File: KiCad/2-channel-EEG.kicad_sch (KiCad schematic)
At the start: 77 parts, among them J1 Power_Input, J10 ADC_Data, J11 ISO_IN_C, J12 CH1_AVG_EN, J13 MCU_Data, J14 CH2_AVG_EN, J2 Nucleo_3.3, J3 Electrode_Input, J4 GND_select, J7 Conn_02x01, J8 Conn_02x01, J9 ADC_23, SW1 SW_Push_SPDT, U1 PESE1-S5-S5-M-TR, U10 AD8606, U11 ISO6763-Q1, U2 AD8237, U3 AD8237, U4 AD8606, U5 AD8606, U6 TCR2EF33, U7 AD8606, U8 AD8606, U9 MCP3562R

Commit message: drl filter, additional caps for adc, Rs for adc spi.
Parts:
- removed R20: 2M, Resistor_SMD:R_0805_2012Metric_Pad1.20x1.40mm_HandSolder, symbol Device:R_US
- added C19, C25: 10u, Capacitor_SMD:C_0805_2012Metric_Pad1.18x1.45mm_HandSolder, symbol Device:C_Small
- added C27: 1u, Capacitor_SMD:C_0805_2012Metric_Pad1.18x1.45mm_HandSolder, symbol Device:C_Small
- added R23, R24, R25, R26, R27, R28: 10, Resistor_SMD:R_0805_2012Metric_Pad1.20x1.40mm_HandSolder, symbol Device:R_US
- added R29: 1M, Resistor_SMD:R_0805_2012Metric_Pad1.20x1.40mm_HandSolder, symbol Device:R_US
- C17: value C -> 10u
- C18: value 2u -> 10u
- C20: value 1u -> 10u
- R18: value R -> 100
- renumbered C19 to C21, C21 to C22, C22 to C23, C23 to C24, C24 to C26, C25 to C28, J12 to J10, J13 to J11, J14 to J12, J7 to J5, J8 to J6, J9 to J7, J10 to J8, J11 to J9, R21 to R20, R22 to R21, R23 to R22, U9 to U10, U10 to U9
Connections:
- net +3.3V: now also C20.2, C25.2
- net ADC_MCLK: now also R23.1; no longer U10.18 (MCLK)
- net ADC_SCK: now also R27.1; no longer U10.14 (SCK)
- net ADC_SDI: now also R26.1; no longer U10.15 (SDI)
- net ADC_SDO: now also R25.1; no longer U10.16 (SDO)
- net ADC_~{CS}: now also R28.1; no longer U10.13 (~{CS})
- net ADC_~{IRQ}: now also R24.1; no longer U10.17 (~{IRQ}/MDAT)
- net Driven_GND: now also C22.1, R20.1, R21.1; no longer C20.1
- net GND: now also C20.1, U10.3 (REFIN-), C19.2, C25.1
- net VGND: now also R29.1
- net at J10.1 (Pin_1), J12.1 (Pin_1): now also C27.2; no longer U9.5 (+)
- net at U10.4 (REFIN+/OUT): now also C19.1
- net +3.3V_nucleo renamed +3V3_nucleo
- new net: C27.1, R29.2, U9.5 (+)
- new net: R24.2, U10.17 (~{IRQ}/MDAT)
- new net: R27.2, U10.14 (SCK)
- new net: R26.2, U10.15 (SDI)
- new net: R25.2, U10.16 (SDO)
- new net: R28.2, U10.13 (~{CS})
- new net: R23.2, U10.18 (MCLK)
- no-connect marks 6 -> 4
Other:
- moved on the sheet: C15, C22, C23, J10, J12, R20, R21, R22, RN1, RN2, U7A, U9A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

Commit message: updated DRL and pcb
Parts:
- removed J10: CH1_AVG_EN, Connector_PinHeader_2.54mm:PinHeader_2x01_P2.54mm_Vertical, symbol Connector_Generic:Conn_02x01
- removed J12: CH2_AVG_EN, Connector_PinHeader_2.54mm:PinHeader_2x01_P2.54mm_Vertical, symbol Connector_Generic:Conn_02x01
- removed R20: 60k, Resistor_SMD:R_0805_2012Metric_Pad1.20x1.40mm_HandSolder, symbol Device:R_US
- added C26: 0.1u, Capacitor_SMD:C_0805_2012Metric_Pad1.18x1.45mm_HandSolder, symbol Device:C_Small
- added C29: 1u, Capacitor_SMD:C_0805_2012Metric_Pad1.18x1.45mm_HandSolder, symbol Device:C_Small
- added J7: VGND, Connector_PinHeader_2.54mm:PinHeader_1x01_P2.54mm_Vertical, symbol Connector_Generic:Conn_01x01
- added R22: 10k, Resistor_SMD:R_0805_2012Metric_Pad1.20x1.40mm_HandSolder, symbol Device:R_US
- added R30: 1M, Resistor_SMD:R_0805_2012Metric_Pad1.20x1.40mm_HandSolder, symbol Device:R_US
- added U11: AD8606, Package_SO:MSOP-8_3x3mm_P0.65mm, symbol Senior_Project_Library:AD8606
- renumbered C17 to C16, C18 to C17, C16 to C18, C3 to C2, C26 to C27, C27 to C28, C2 to C3, C28 to C30, C7 to C6, C6 to C7, J9 to J10, J7 to J8, J8 to J9, R3 to R1, R16 to R14, R17 to R15, R14 to R16, R15 to R17, R4 to R2, R21 to R20, R22 to R21, R1 to R3, R2 to R4, R6 to R5, R5 to R6, R8 to R7, R7 to R8, U11 to U12, U3 to U2, U2 to U3, U5 to U4, U4 to U5
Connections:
- net +3.3V: now also C26.2, U11.8 (V+)
- net CH1+: now also J3.4 (Pin_4), RN2.3, U2.2 (+); no longer J3.5 (Pin_5), RN1.3, U3.2 (+)
- net CH1-: now also J3.5 (Pin_5), RN2.4, U2.3 (-); no longer J3.4 (Pin_4), RN1.4, U3.3 (-)
- net CH1_AO: now also C16.2, R18.1; no longer C17.2, R19.1
- net CH2+: now also J3.1 (Pin_1), RN1.3, U3.2 (+); no longer J3.2 (Pin_2), RN2.3, U2.2 (+)
- net CH2-: now also J3.2 (Pin_2), RN1.4, U3.3 (-); no longer J3.1 (Pin_1), RN2.4, U2.3 (-)
- net CH2_AO: now also C17.2, R19.1; no longer C16.2, R18.1
- net Driven_GND: now also U9.1
- net GND: now also C26.1, U11.4 (V-), U11.5 (+)
- net VGND: now also J4.3 (Pin_4), J7.1 (Pin_1), R30.1; no longer J4.4 (Pin_4)
- net at C28.2: now also RN1.1, RN1.2
- net at C22.2, R20.2, U9.2 (-): now also R21.2, R22.1; no longer R21.1
- net at U9.6 (-), U9.7: now also R21.1; no longer R21.2
- net at RN2.1, RN2.2: now also C29.2
- new net: R22.2, U11.1, U11.2 (-)
- new net: U11.6 (-), U11.7
- new net: C29.1, R30.2, U11.3 (+)
- no-connect marks 4 -> 3
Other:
- moved on the sheet: C10, C11, C13, C14, C15, C16, C17, C19, C2, C20, C21, C22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

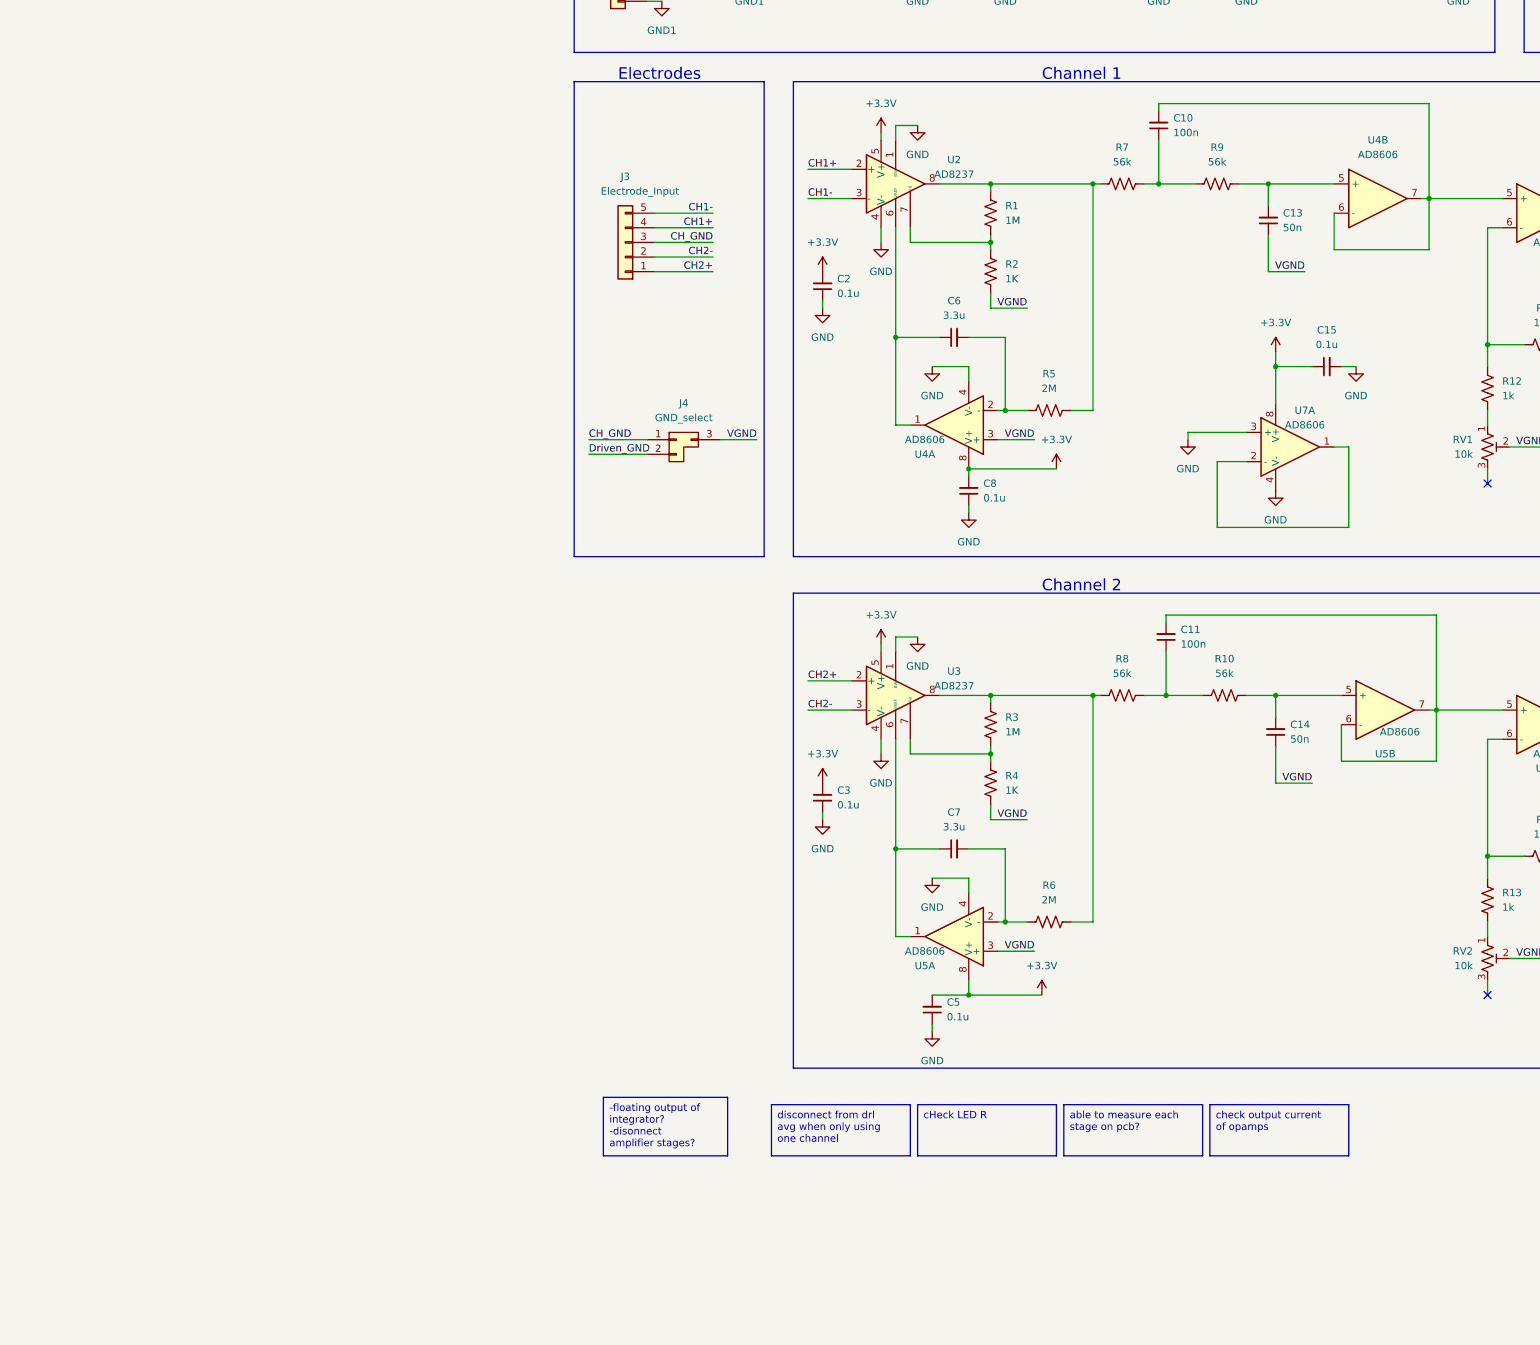
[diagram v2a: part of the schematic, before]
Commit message: added solder jumpers between INA and filter
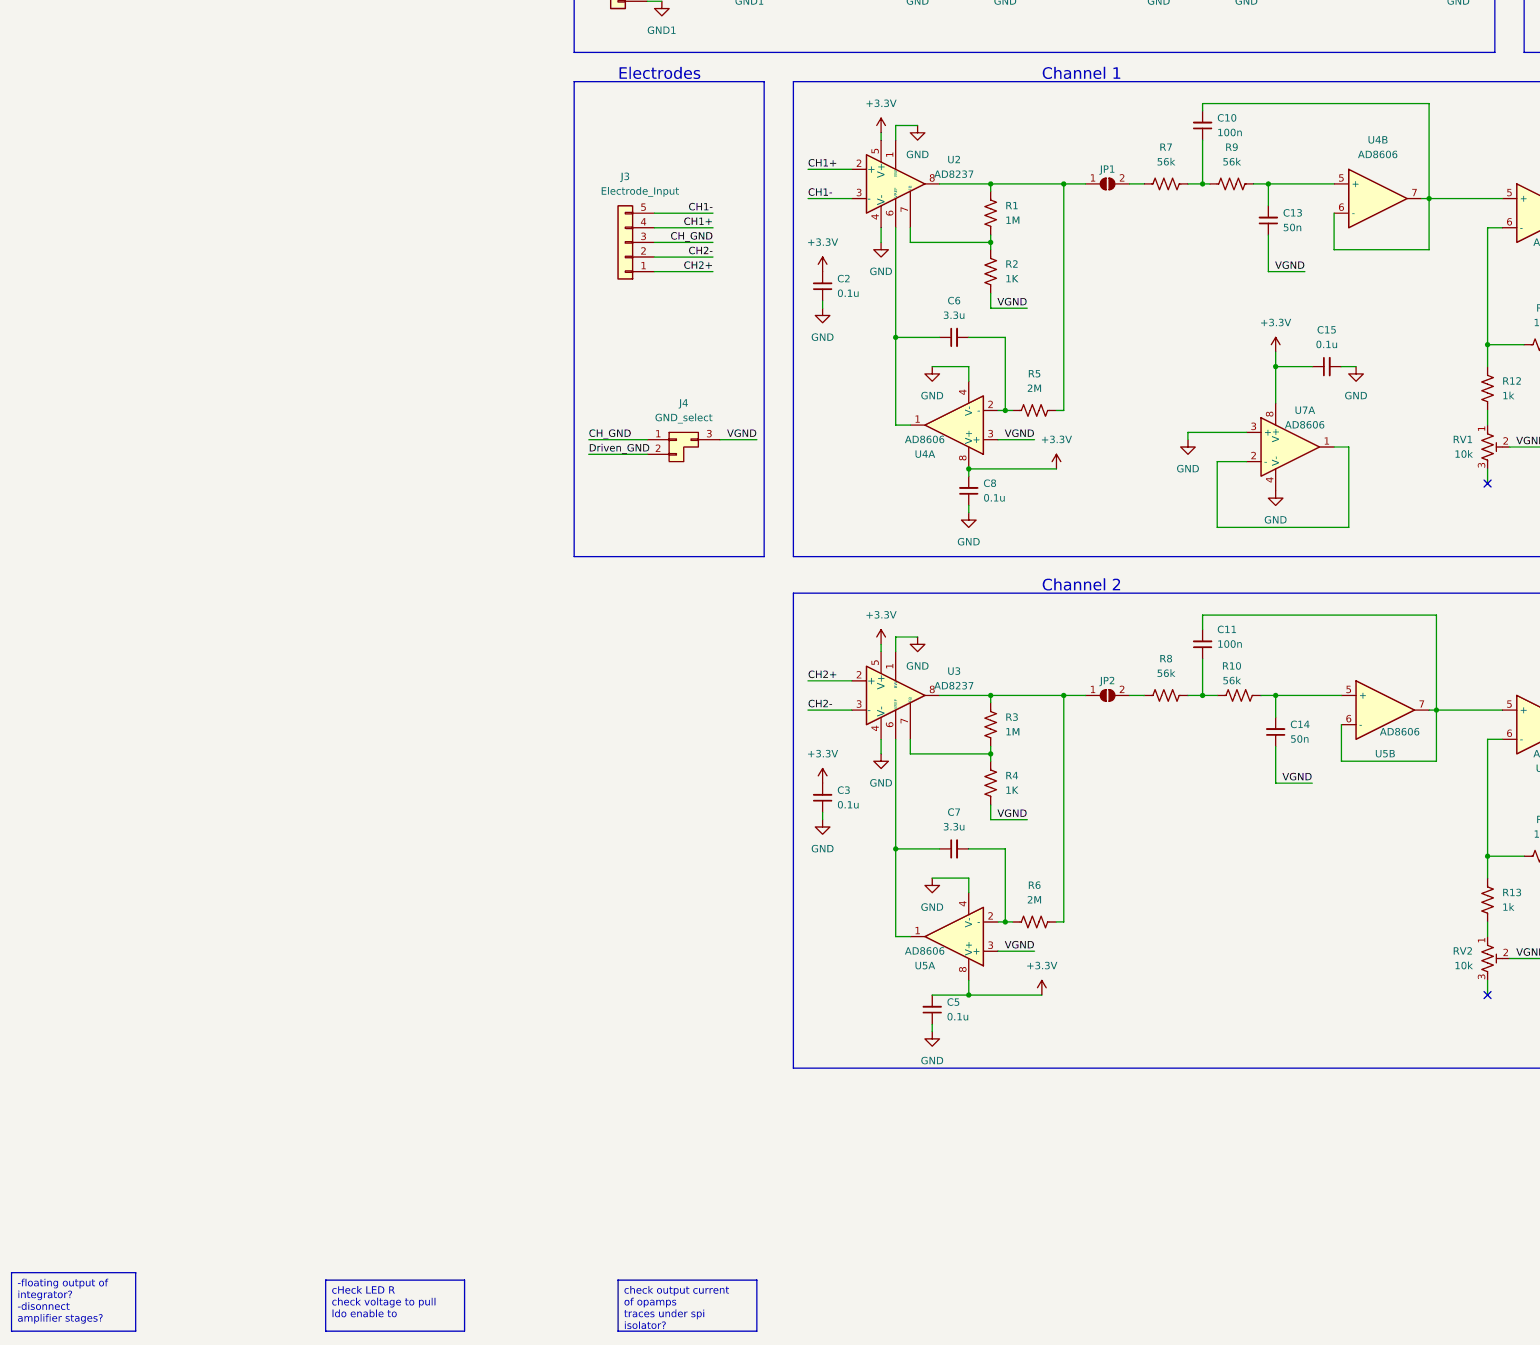
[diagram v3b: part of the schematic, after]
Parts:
- added JP1, JP2: SolderJumper_2_Open, Resistor_SMD:R_0603_1608Metric, symbol Jumper:SolderJumper_2_Open
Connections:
- net at R3.1, R6.2, U3.8: now also JP2.1 (A); no longer R8.2
- net at R1.1, R5.2, U2.8: now also JP1.1 (A); no longer R7.2
- new net: JP2.2 (B), R8.2
- new net: JP1.2 (B), R7.2
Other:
- moved on the sheet: C10, C11, R10, R5, R6, R7, R8, R9

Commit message: fix wrong reference C,R values
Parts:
- C10, C11: value 100n -> 0.1u
- C13, C14: value 50n -> 47n
- C6, C7: value 3.3u -> 10u
- R11: value 10k -> 510
- R5, R6: value 2M -> 3M
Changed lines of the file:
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@@
     (fill (type none))
   )
-  (text_box "cHeck LED R\ncheck voltage to pull ldo enable to\n"
-    (at -24.13 274.32 0) (size 24.13 8.89)
+  (text_box "cHeck LED R\n\n"
+    (at -78.74 284.48 0) (size 24.13 8.89)
     (stroke (width 0) (type default))
     (fill (type none))
@@
   )
   (text_box "check output current of opamps\ntraces under spi isolator?\n"
-    (at 26.67 274.32 0) (size 24.13 8.89)
-    (stroke (width 0) (type default))
-    (fill (type none))
-    (effects (font (size 1.27 1.27)) (justify left top))
-  )
-  (text_box "-floating output of integrator?\n-disonnect amplifier stages?"
-    (at -78.74 273.05 0) (size 21.59 10.16)
+    (at -78.74 294.64 0) (size 24.13 8.89)
     (stroke (width 0) (type default))
     (fill (type none))
@@
       (effects (font (size 1.27 1.27)) (justify right))
     )
-    (property "Value" "10k" (at 146.05 39.37 0)
+    (property "Value" "510" (at 146.05 39.37 0)
       (effects (font (size 1.27 1.27)) (justify right))
     )
@@
       (effects (font (size 1.27 1.27)) (justify right))
     )
-    (property "Value" "100n" (at 130.81 163.83 0)
+    (property "Value" "0.1u" (at 130.81 163.83 0)
       (effects (font (size 1.27 1.27)) (justify right))
     )
@@
       (effects (font (size 1.27 1.27)))
     )
-    (property "Value" "2M" (at 99.06 208.28 90)
+    (property "Value" "3M" (at 99.06 208.28 90)
       (effects (font (size 1.27 1.27)))
     )
@@
       (effects (font (size 1.27 1.27)) (justify right))
     )
-    (property "Value" "50n" (at 143.51 180.3336 0)
+    (property "Value" "47n" (at 143.51 180.3336 0)
       (effects (font (size 1.27 1.27)) (justify right))
     )
@@
       (effects (font (size 1.27 1.27)))
     )
-    (property "Value" "2M" (at 99.06 119.38 90)
+    (property "Value" "3M" (at 99.06 119.38 90)
       (effects (font (size 1.27 1.27)))
     )
@@
       (effects (font (size 1.27 1.27)))
     )
-    (property "Value" "3.3u" (at 85.0963 106.68 90)
+    (property "Value" "10u" (at 85.0963 106.68 90)
       (effects (font (size 1.27 1.27)))
     )
@@
       (effects (font (size 1.27 1.27)) (justify right))
     )
-    (property "Value" "50n" (at 142.24 91.4336 0)
+    (property "Value" "47n" (at 142.24 91.4336 0)
       (effects (font (size 1.27 1.27)) (justify right))
     )
@@
       (effects (font (size 1.27 1.27)))
     )
-    (property "Value" "3.3u" (at 85.0963 195.58 90)
+    (property "Value" "10u" (at 85.0963 195.58 90)
       (effects (font (size 1.27 1.27)))
     )
@@
       (effects (font (size 1.27 1.27)) (justify right))
     )
-    (property "Value" "100n" (at 130.81 74.9236 0)
+    (property "Value" "0.1u" (at 130.81 74.9236 0)
       (effects (font (size 1.27 1.27)) (justify right))
     )

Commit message: schematic BOM
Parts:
- R1: LCSC Part (none) -> C2074251
- R10, R7, R8, R9: value 56k -> 56.2k
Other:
- moved on the sheet: C5
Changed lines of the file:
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@@
     (stroke (width 0) (type default))
   )
-  (wire (pts (xy 81.28 229.87) (xy 81.28 231.14))
+  (wire (pts (xy 87.63 229.87) (xy 87.63 231.14))
     (stroke (width 0) (type default))
   )
@@
     (stroke (width 0) (type default))
   )
-  (wire (pts (xy 81.28 224.79) (xy 87.63 224.79))
-    (stroke (width 0) (type default))
-  )
   (wire (pts (xy 251.46 95.25) (xy 251.46 93.98))
     (stroke (width 0) (type default))
@@
     (fill (type none))
   )
-  (text_box "cHeck LED R\n\n"
-    (at -78.74 284.48 0) (size 24.13 8.89)
-    (stroke (width 0) (type default))
-    (fill (type none))
-    (effects (font (size 1.27 1.27)) (justify left top))
-  )
-  (text_box "check output current of opamps\ntraces under spi isolator?\n"
-    (at -78.74 294.64 0) (size 24.13 8.89)
+  (text_box "check output current of opamps\ntraces under spi isolator?\nDRL resistor for gain\n\n"
+    (at 19.05 269.24 0) (size 24.13 12.7)
     (stroke (width 0) (type default))
     (fill (type none))
@@
     )
   )
-  (symbol (lib_id "Device:C_Small") (at 81.28 227.33 180) (unit 1)
+  (symbol (lib_id "Device:C_Small") (at 87.63 227.33 180) (unit 1)
     (in_bom yes) (on_board yes) (dnp no) (fields_autoplaced)
-    (property "Reference" "C5" (at 83.82 226.0536 0)
+    (property "Reference" "C5" (at 90.17 226.0536 0)
       (effects (font (size 1.27 1.27)) (justify right))
     )
-    (property "Value" "0.1u" (at 83.82 228.5936 0)
+    (property "Value" "0.1u" (at 90.17 228.5936 0)
       (effects (font (size 1.27 1.27)) (justify right))
     )
-    (property "Footprint" "Capacitor_SMD:C_0805_2012Metric_Pad1.18x1.45mm_HandSolder" (at 81.28 227.33 0)
+    (property "Footprint" "Capacitor_SMD:C_0805_2012Metric_Pad1.18x1.45mm_HandSolder" (at 87.63 227.33 0)
       (effects (font (size 1.27 1.27)) hide)
     )
-    (property "Datasheet" "~" (at 81.28 227.33 0)
+    (property "Datasheet" "~" (at 87.63 227.33 0)
       (effects (font (size 1.27 1.27)) hide)
     )
@@
       (effects (font (size 1.27 1.27)) hide)
     )
+    (property "LCSC Part" "C2074251" (at 91.44 88.9 0)
+      (effects (font (size 1.27 1.27)) hide)
+    )
     (pin "1")
     (pin "2")
@@
     )
   )
-  (symbol (lib_id "power:GND") (at 81.28 231.14 0) (mirror y) (unit 1)
+  (symbol (lib_id "power:GND") (at 87.63 231.14 0) (mirror y) (unit 1)
     (in_bom yes) (on_board yes) (dnp no)
-    (property "Reference" "#PWR021" (at 81.28 237.49 0)
+    (property "Reference" "#PWR021" (at 87.63 237.49 0)
       (effects (font (size 1.27 1.27)) hide)
     )
-    (property "Value" "GND" (at 81.28 236.22 0)
+    (property "Value" "GND" (at 87.63 236.22 0)
       (effects (font (size 1.27 1.27)))
     )
-    (property "Footprint" "" (at 81.28 231.14 0)
+    (property "Footprint" "" (at 87.63 231.14 0)
       (effects (font (size 1.27 1.27)) hide)
     )
-    (property "Datasheet" "" (at 81.28 231.14 0)
+    (property "Datasheet" "" (at 87.63 231.14 0)
       (effects (font (size 1.27 1.27)) hide)
     )
@@
       (effects (font (size 1.27 1.27)))
     )
-    (property "Value" "56k" (at 133.35 170.18 90)
+    (property "Value" "56.2k" (at 133.35 170.18 90)
       (effects (font (size 1.27 1.27)))
     )
@@
       (effects (font (size 1.27 1.27)))
     )
-    (property "Value" "56k" (at 121.92 80.01 90)
+    (property "Value" "56.2k" (at 121.92 80.01 90)
       (effects (font (size 1.27 1.27)))
     )
@@
       (effects (font (size 1.27 1.27)))
     )
-    (property "Value" "56k" (at 121.92 168.91 90)
+    (property "Value" "56.2k" (at 121.92 168.91 90)
       (effects (font (size 1.27 1.27)))
     )
@@
       (effects (font (size 1.27 1.27)))
     )
-    (property "Value" "56k" (at 133.35 80.01 90)
+    (property "Value" "56.2k" (at 133.35 80.01 90)
       (effects (font (size 1.27 1.27)))
     )
